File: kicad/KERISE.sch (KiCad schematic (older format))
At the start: 20 parts, among them P1 ANT, SW1 SW_Push, U1 FLASH, U2 ESP32, U3 XTAL

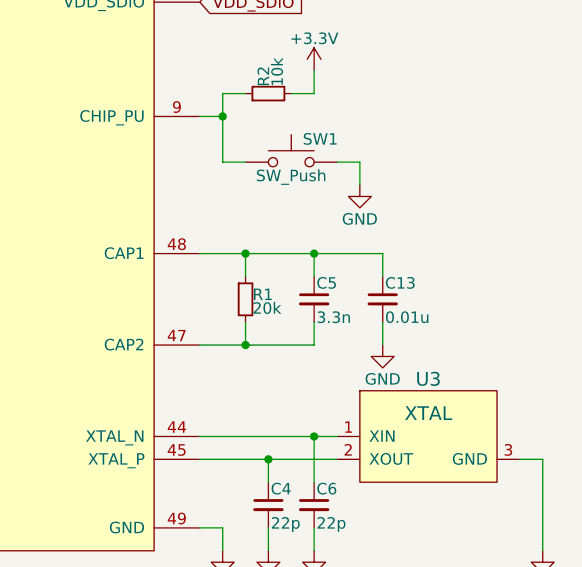
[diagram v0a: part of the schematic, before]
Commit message: 自動配線1残し
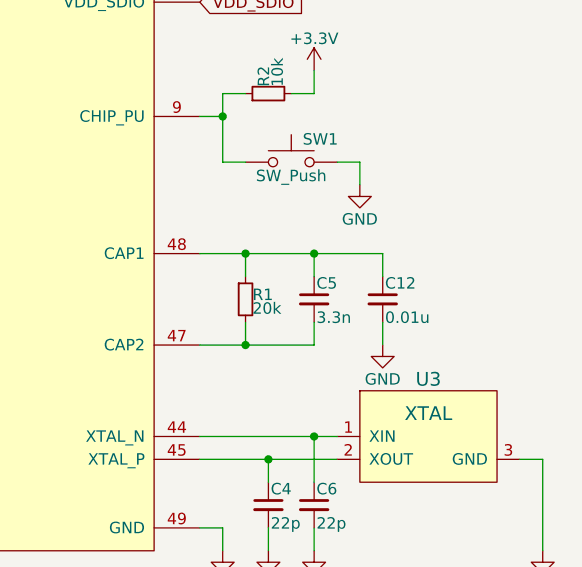
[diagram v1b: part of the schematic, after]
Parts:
- renumbered C13 to C12
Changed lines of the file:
@@
 $EndComp
 $Comp
-L C_Small C13
+L C_Small C12
 U 1 1 58A770D7
 P 9300 3900
-F 0 "C13" H 9310 3970 50  0000 L CNN
+F 0 "C12" H 9310 3970 50  0000 L CNN
 F 1 "0.01u" H 9310 3820 50  0000 L CNN
 F 2 "Capacitors_SMD:C_0201" H 9300 3900 50  0001 C CNN

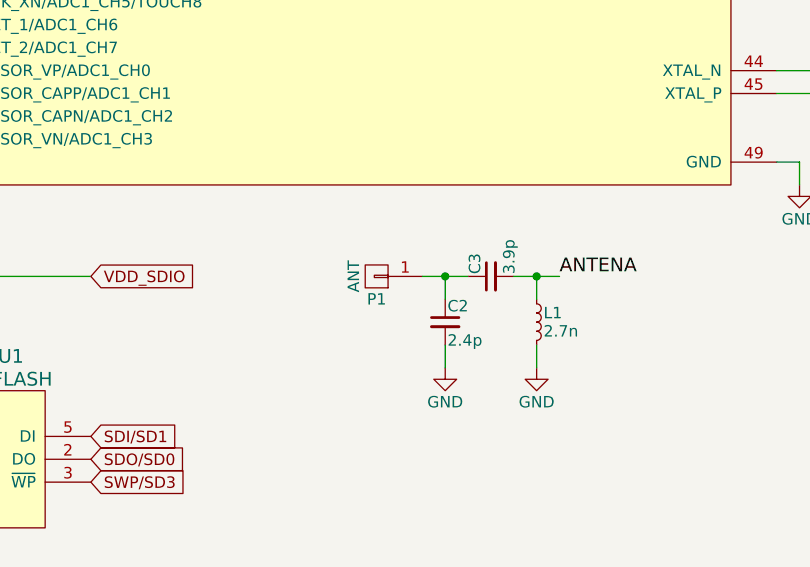
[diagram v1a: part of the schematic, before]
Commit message: 実装経験をもとにフットプリントを改良，ミスを修正
SC70サイズのオペアンプのピンアサインを修正
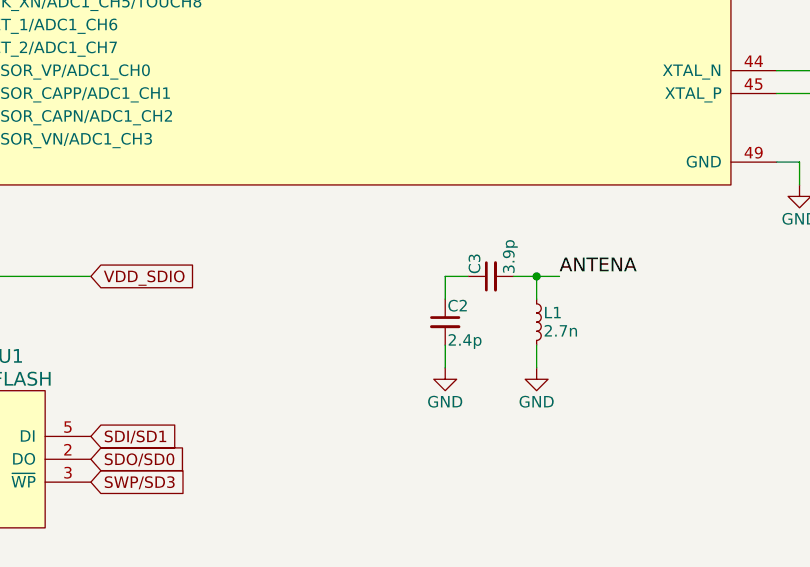
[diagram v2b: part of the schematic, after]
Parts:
- removed P1: ANT, mouse:SMD_conn_1, symbol CONN_01X01
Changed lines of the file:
@@
 $EndComp
 $Comp
-L GND #PWR01
+L GND #PWR6
 U 1 1 589812A6
 P 8600 5000
-F 0 "#PWR01" H 8600 4750 50  0001 C CNN
+F 0 "#PWR6" H 8600 4750 50  0001 C CNN
 F 1 "GND" H 8600 4850 50  0000 C CNN
 F 2 "" H 8600 5000 50  0000 C CNN
@@
 BUTTON
 $Comp
-L GND #PWR02
+L GND #PWR11
 U 1 1 58964ED8
 P 9200 3400
-F 0 "#PWR02" H 9200 3150 50  0001 C CNN
+F 0 "#PWR11" H 9200 3150 50  0001 C CNN
 F 1 "GND" H 9200 3250 50  0000 C CNN
 F 2 "" H 9200 3400 50  0000 C CNN
@@
 UART-RX
 $Comp
-L +3.3V #PWR03
+L +3.3V #PWR9
 U 1 1 58A4281C
 P 9000 2900
-F 0 "#PWR03" H 9000 2750 50  0001 C CNN
+F 0 "#PWR9" H 9000 2750 50  0001 C CNN
 F 1 "+3.3V" H 9000 3040 50  0000 C CNN
 F 2 "" H 9000 2900 50  0000 C CNN
@@
 $EndComp
 $Comp
-L GND #PWR04
+L GND #PWR12
 U 1 1 58A70C45
 P 9300 2300
-F 0 "#PWR04" H 9300 2050 50  0001 C CNN
+F 0 "#PWR12" H 9300 2050 50  0001 C CNN
 F 1 "GND" H 9300 2150 50  0000 C CNN
 F 2 "" H 9300 2300 50  0000 C CNN
@@
 $EndComp
 $Comp
-L GND #PWR05
+L GND #PWR13
 U 1 1 58A78155
 P 9300 4100
-F 0 "#PWR05" H 9300 3850 50  0001 C CNN
+F 0 "#PWR13" H 9300 3850 50  0001 C CNN
 F 1 "GND" H 9300 3950 50  0000 C CNN
 F 2 "" H 9300 4100 50  0000 C CNN
@@
 $EndComp
 $Comp
-L +3.3V #PWR06
+L +3.3V #PWR5
 U 1 1 58A831D9
 P 8600 900
-F 0 "#PWR06" H 8600 750 50  0001 C CNN
+F 0 "#PWR5" H 8600 750 50  0001 C CNN
 F 1 "+3.3V" H 8600 1040 50  0000 C CNN
 F 2 "" H 8600 900 50  0000 C CNN
@@
 VDD_SDIO
 $Comp
-L GND #PWR07
+L GND #PWR1
 U 1 1 58ABF34A
 P 4400 5800
-F 0 "#PWR07" H 4400 5550 50  0001 C CNN
+F 0 "#PWR1" H 4400 5550 50  0001 C CNN
 F 1 "GND" H 4400 5650 50  0000 C CNN
 F 2 "" H 4400 5800 50  0000 C CNN
@@
 $EndComp
 $Comp
-L GND #PWR08
+L GND #PWR2
 U 1 1 58ABFAF3
 P 5000 6800
-F 0 "#PWR08" H 5000 6550 50  0001 C CNN
+F 0 "#PWR2" H 5000 6550 50  0001 C CNN
 F 1 "GND" H 5000 6650 50  0000 C CNN
 F 2 "" H 5000 6800 50  0000 C CNN
@@
 $EndComp
 $Comp
-L GND #PWR09
+L GND #PWR7
 U 1 1 58AE002B
 P 8800 5000
-F 0 "#PWR09" H 8800 4750 50  0001 C CNN
+F 0 "#PWR7" H 8800 4750 50  0001 C CNN
 F 1 "GND" H 8800 4850 50  0000 C CNN
 F 2 "" H 8800 5000 50  0000 C CNN
@@
 $EndComp
 $Comp
-L GND #PWR010
+L GND #PWR10
 U 1 1 58AE013E
 P 9000 5000
-F 0 "#PWR010" H 9000 4750 50  0001 C CNN
+F 0 "#PWR10" H 9000 4750 50  0001 C CNN
 F 1 "GND" H 9000 4850 50  0000 C CNN
 F 2 "" H 9000 5000 50  0000 C CNN
@@
 $EndComp
 $Comp
-L GND #PWR011
+L GND #PWR14
 U 1 1 58AE4207
 P 10000 5000
-F 0 "#PWR011" H 10000 4750 50  0001 C CNN
+F 0 "#PWR14" H 10000 4750 50  0001 C CNN
 F 1 "GND" H 10000 4850 50  0000 C CNN
 F 2 "" H 10000 5000 50  0000 C CNN
@@
 $EndComp
 $Comp
-L GND #PWR012
+L GND #PWR3
 U 1 1 5932BFDB
 P 7050 5800
-F 0 "#PWR012" H 7050 5550 50  0001 C CNN
+F 0 "#PWR3" H 7050 5550 50  0001 C CNN
 F 1 "GND" H 7050 5650 50  0000 C CNN
 F 2 "" H 7050 5800 50  0000 C CNN
@@
 $EndComp
 $Comp
-L GND #PWR013
+L GND #PWR4
 U 1 1 5932C0CF
 P 7450 5800
-F 0 "#PWR013" H 7450 5550 50  0001 C CNN
+F 0 "#PWR4" H 7450 5550 50  0001 C CNN
 F 1 "GND" H 7450 5650 50  0000 C CNN
 F 2 "" H 7450 5800 50  0000 C CNN
@@
 	1    0    0    -1
 $EndComp
-$Comp
-L CONN_01X01 P1
-U 1 1 5932D0A3
-P 6750 5400
-F 0 "P1" H 6750 5500 50  0000 C CNN
-F 1 "ANT" V 6850 5400 50  0000 C CNN
-F 2 "mouse:SMD_conn_1" H 6750 5400 50  0001 C CNN
-F 3 "" H 6750 5400 50  0000 C CNN
-	1    6750 5400
-	-1   0    0    1
-$EndComp
-Wire Wire Line
-	6950 5400 7150 5400
-Wire Wire Line
-	7050 5400 7050 5500
-Connection ~ 7050 5400
 Wire Wire Line
 	7050 5700 7050 5800
@@
 	1400 1600 1500 1600
 $Comp
-L VDDA #PWR014
+L VDDA #PWR8
 U 1 1 59C3BA09
 P 8900 900
-F 0 "#PWR014" H 8900 750 50  0001 C CNN
+F 0 "#PWR8" H 8900 750 50  0001 C CNN
 F 1 "VDDA" H 8900 1050 50  0000 C CNN
 F 2 "" H 8900 900 50  0001 C CNN
@@
 Wire Wire Line
 	8600 2200 8500 2200
+Wire Wire Line
+	7050 5500 7050 5400
+Wire Wire Line
+	7050 5400 7150 5400
 $EndSCHEMATC
